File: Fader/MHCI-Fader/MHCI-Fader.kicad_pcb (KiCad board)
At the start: 2 copper layers, 107.5 x 20 mm, 30 parts, among them J1 Conn_01x06, J2 Conn_01x03, SW1 SW_Push_LED, U1 TJA1051T, U3 SRV05-4

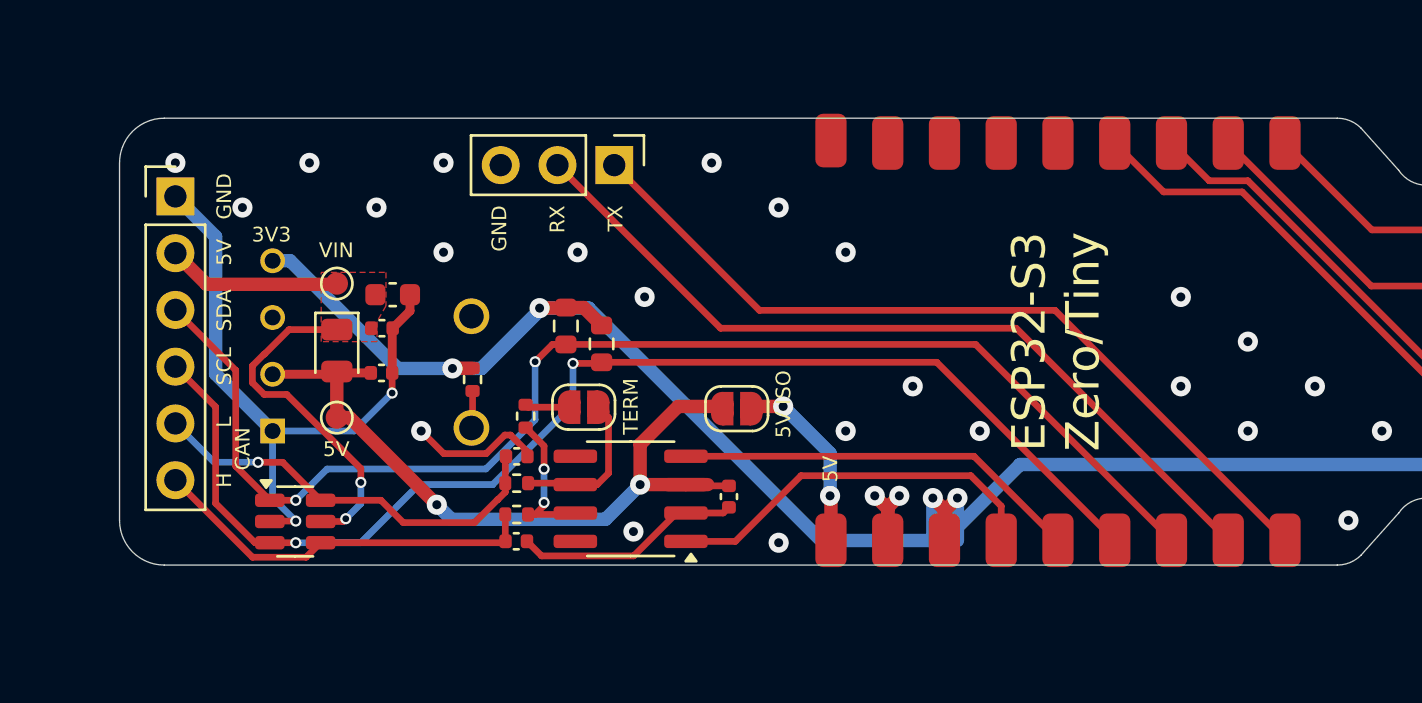
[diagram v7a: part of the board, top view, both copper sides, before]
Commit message: MHCI Fader - Add logic level converter and re-route traces
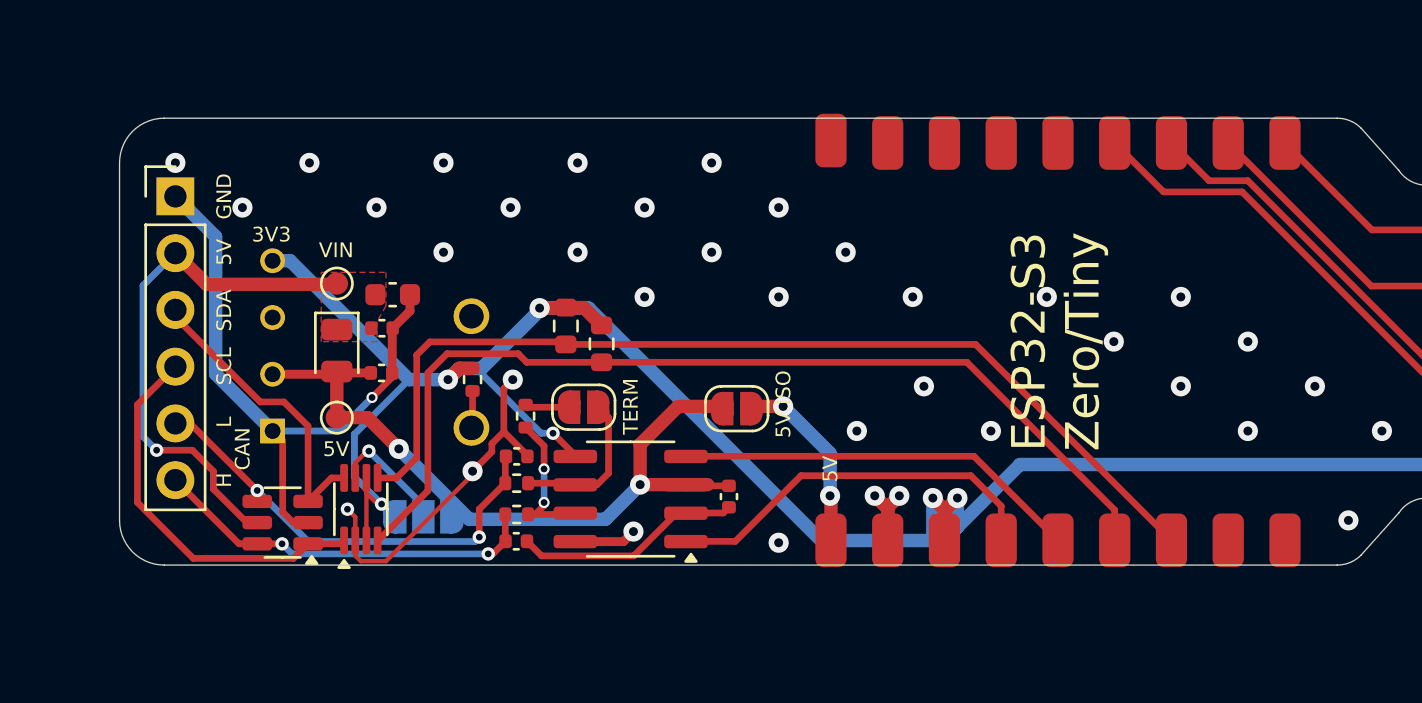
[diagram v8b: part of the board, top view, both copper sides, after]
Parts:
- removed J2: Conn_01x03, Connector_PinHeader_2.54mm:PinHeader_1x03_P2.54mm_Vertical
- removed U1: TJA1051T, Package_SO:SOIC-8_3.9x4.9mm_P1.27mm
- added JP3: SolderJumper_3_Open, Jumper:SolderJumper-3_P1.3mm_Open_RoundedPad1.0x1.5mm, B.Cu at (84.1, 109.8)
- added U4: TXB0102DCU, Package_SO:VSSOP-8_2.3x2mm_P0.5mm, F.Cu at (81.3, 109.5)
- added U5: TJA1051T-3, Package_SO:SOIC-8_3.9x4.9mm_P1.27mm, F.Cu at (93.4, 109.0)
- moved U3 0.56 mm to (77.8, 110.1), turned to 180 degrees
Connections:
- J1 pad 3: SDA -> SDA_5
- J1 pad 4: SCL -> SCL_5
- U2 pad 5: DMX- -> /ESP_32_GPIO_05
- U2 pad 6: DMX+ -> /ESP_32_GPIO_06
- U3 pad 1: SDA -> SCL_5
- U3 pad 3: SCL -> SDA_5
- U3 pad 4: CANH -> CANL
- U3 pad 6: CANL -> CANH
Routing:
- net DMX-: track 37.0 -> 0.00 mm
- net DMX+: track 37.0 -> 0.00 mm
- net +3V3: track 122.7 -> 142.0 mm, vias 5 -> 7
- net SCL_5: track 0.00 -> 17.4 mm
- net SDA: track 58.7 -> 44.4 mm, vias 2 -> 0
- net SDA_5: track 0.00 -> 13.7 mm
- net GND: track 22.7 -> 35.2 mm, vias 48 -> 58
- net SCL: track 55.5 -> 43.8 mm, vias 2 -> 0
- net Net-(JP3-C): track 0.00 -> 5.46 mm, vias 0 -> 1
- net CANL: track 18.8 -> 20.7 mm, vias 1 -> 2
- net Earth: track 28.7 -> 28.0 mm, vias 2 -> 1
- net VIN: track 23.2 -> 23.8 mm, vias 2 -> 1
- net CANH: track 17.7 -> 17.6 mm, vias 0 -> 2
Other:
- board text added: "TOOLING HOLES MOUNTING HOLES"
- board text removed: "RX"
- board text removed: "TX"
